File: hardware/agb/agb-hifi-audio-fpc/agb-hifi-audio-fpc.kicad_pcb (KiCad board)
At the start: 2 copper layers, 23.1 x 34.8 mm, 4 parts, among them J1 AGB_AMP_CONNECT, J4 PAIR, J5 BOARD_CONNECT

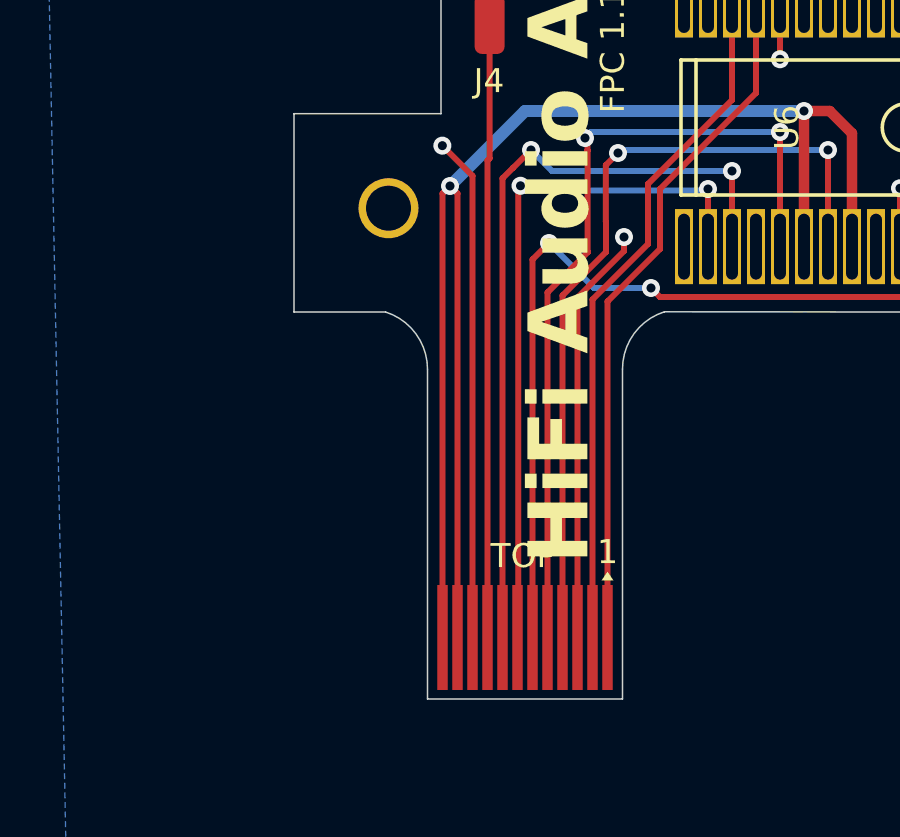
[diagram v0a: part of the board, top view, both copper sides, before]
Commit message: hardware(agb): single 0.4mm VBAT run down the lead, solid zone pad connection
Replace the two parallel 0.2 mm VBAT traces down the connector lead (x=83.05 and
x=83.55, y108.65-124) with one 0.4 mm trace on the centreline (x=83.3,
y108.4-121.4), fanning back out to the two J5 fingers with 0.2 mm 45-degree stubs
at y121.4-123.45. Zone pad connection goes from thermal reliefs to solid
(connect_pads yes, pad_connection 2 in the .kicad_pro). DRC clean, 0
unconnected.
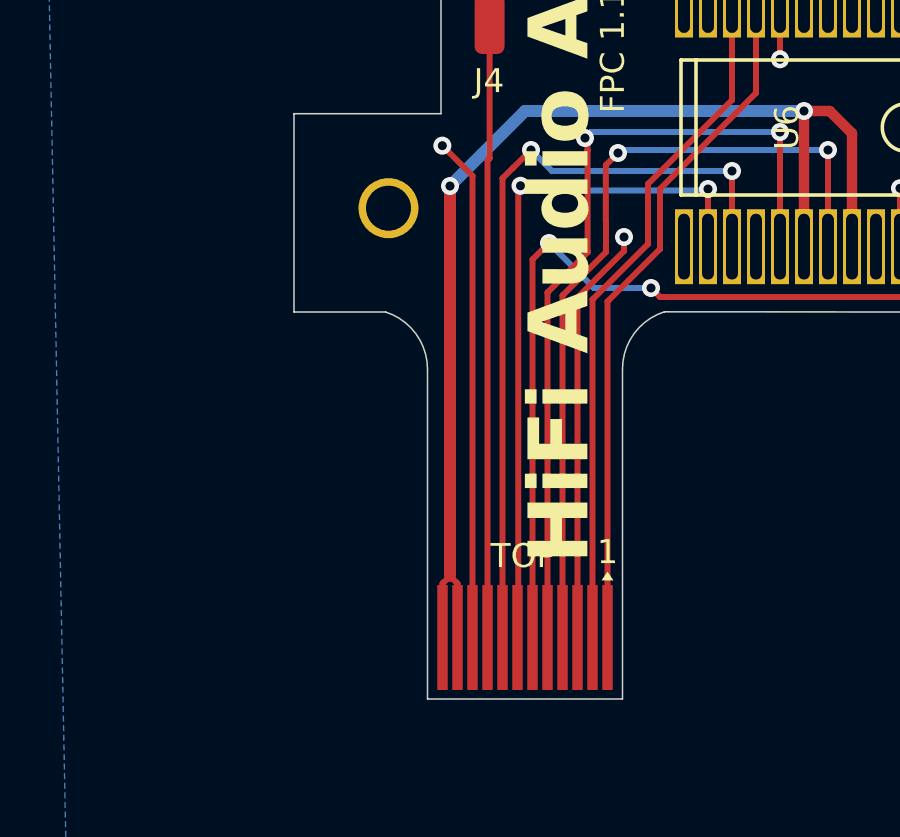
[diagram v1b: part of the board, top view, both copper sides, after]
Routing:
- net VBAT: track 54.4 -> 40.3 mm
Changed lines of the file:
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@@
 	)
 	(segment
-		(start 83.55 108.65)
-		(end 83.3 108.4)
+		(start 83.05 123.45)
+		(end 83.05 121.65)
 		(width 0.2)
 		(layer "F.Cu")
@@
 	)
 	(segment
-		(start 83.55 108.65)
-		(end 83.55 124)
-		(width 0.2)
+		(start 83.3 108.4)
+		(end 83.3 121.4)
+		(width 0.4)
 		(layer "F.Cu")
 		(net "VBAT")
@@
 	)
 	(segment
-		(start 83.05 108.65)
-		(end 83.05 124)
-		(width 0.2)
-		(layer "F.Cu")
-		(net "VBAT")
-	)
-	(segment
 		(start 96.7 106.645405)
 		(end 96.7 110.42132)
@@
 	)
 	(segment
-		(start 83.05 108.65)
-		(end 83.3 108.4)
+		(start 83.55 123.45)
+		(end 83.55 121.65)
 		(width 0.2)
 		(layer "F.Cu")
@@
 		(end 95.954595 105.9)
 		(width 0.35)
+		(layer "F.Cu")
+		(net "VBAT")
+	)
+	(segment
+		(start 83.05 121.65)
+		(end 83.3 121.4)
+		(width 0.2)
+		(layer "F.Cu")
+		(net "VBAT")
+	)
+	(segment
+		(start 83.55 121.65)
+		(end 83.3 121.4)
+		(width 0.2)
 		(layer "F.Cu")
 		(net "VBAT")
@@
 		(polygon
 			(pts
-				(xy 89.057722 121.938927) (xy 82.547882 121.934437) (xy 82.55214 126.740399) (xy 89.042278 126.761185)
+				(xy 89.057722 120.698528) (xy 82.547882 120.694038) (xy 82.55214 125.5) (xy 89.042278 125.520786)
 			)
 		)
@@
 		(layer "B.Cu")
 		(hatch edge 0.5)
-		(connect_pads
+		(connect_pads yes
 			(clearance 0.1)
 		)
